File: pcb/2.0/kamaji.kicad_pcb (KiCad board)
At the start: 2 copper layers, 100 x 100 mm, 87 parts, among them J1 RJ10, J2 RJ10, J3 RJ10, J4 RJ10, J5 RJ10, J6 RJ10, J7 USB_B, J8 USB_A, Q1 2N3904, Q2 IRL540N, Q3 IRL540N, SW1 SW_Push, SW2 SW_Push, SW3 SW_Push, U1 ATMEGA32U4-AU, Y1 16MHz

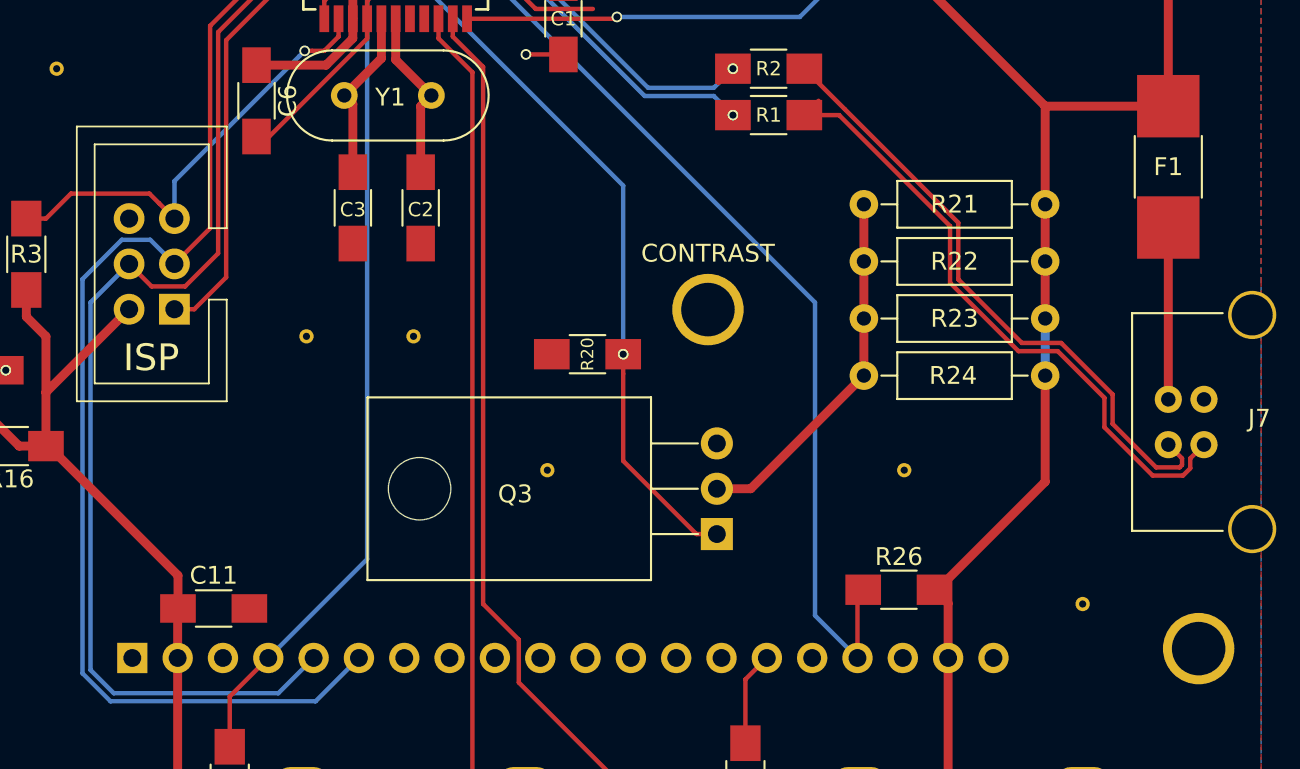
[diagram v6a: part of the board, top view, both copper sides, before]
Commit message: reroute the differential pair
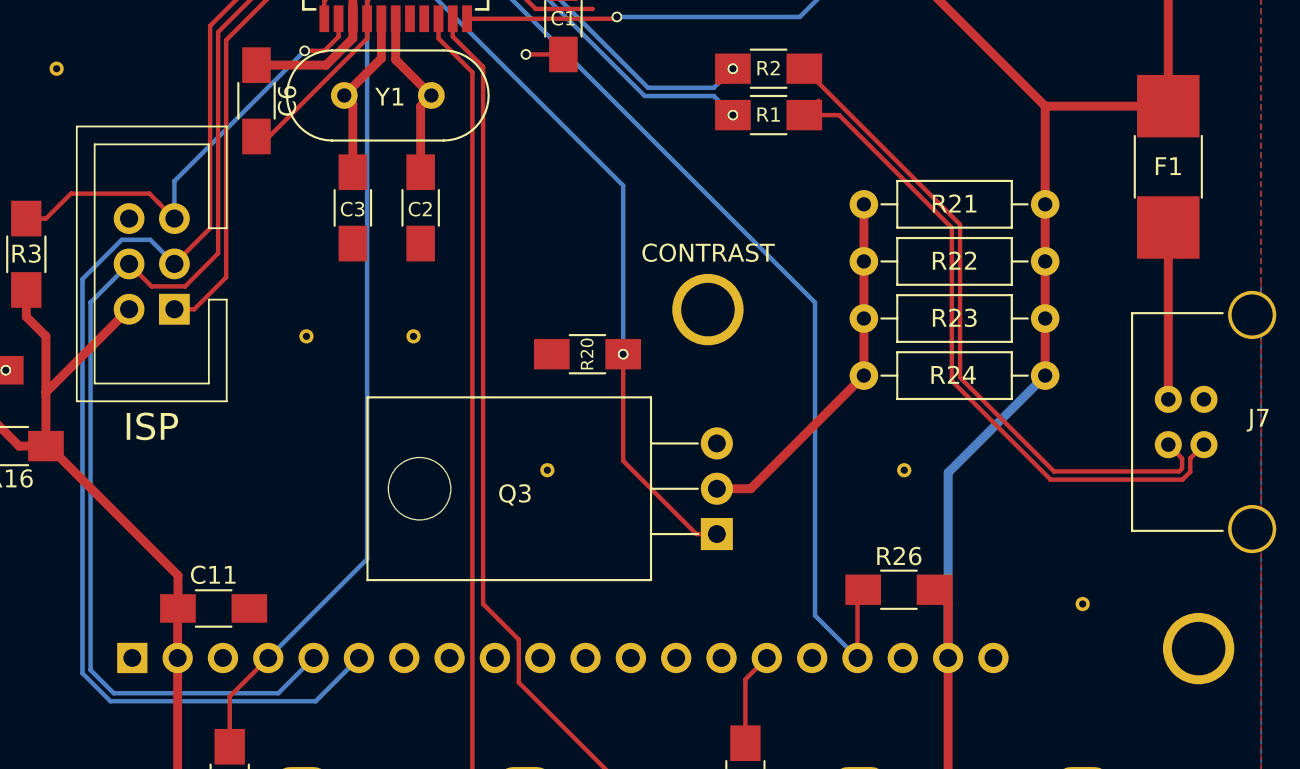
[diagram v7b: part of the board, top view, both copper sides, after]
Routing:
- net VCC: track 265.3 -> 268.9 mm
- net /USBBD-: track 34.8 -> 37.3 mm
- net /USBBD+: track 35.8 -> 38.3 mm
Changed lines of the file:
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@@
     (thickness 1.6)
     (drawings 15)
-    (tracks 395)
+    (tracks 387)
     (zones 0)
     (modules 87)
@@
     (effects (font (size 1 1) (thickness 0.2)))
   )
-  (gr_text ISP (at 85.3 116.2 360) (layer F.SilkS)
-    (effects (font (size 1.5 1.5) (thickness 0.3)))
+  (gr_text ISP (at 85.3 120.1) (layer F.SilkS)
+    (effects (font (size 1.5 1.5) (thickness 0.25)))
   )
   (gr_text 5V (at 73.25 107.8) (layer F.SilkS)
@@
   (segment (start 72.85 121.1) (end 75.35 121.1) (width 0.25) (layer F.Cu) (net 2))
   (segment (start 75.35 121.1) (end 75.4 121.15) (width 0.25) (layer F.Cu) (net 2))
+  (segment (start 129.961034 133.024284) (end 129.961034 122.638966) (width 0.5) (layer B.Cu) (net 3))
+  (segment (start 129.961034 122.638966) (end 135.4 117.2) (width 0.5) (layer B.Cu) (net 3))
+  (segment (start 135.4 117.2) (end 135.4 114) (width 0.5) (layer F.Cu) (net 3))
   (segment (start 103 85.8) (end 103 84.8) (width 0.5) (layer F.Cu) (net 3))
   (segment (start 103 84.8) (end 104.7 83.1) (width 0.5) (layer F.Cu) (net 3))
@@
   (segment (start 128.5 95.2) (end 109.7 95.2) (width 0.5) (layer F.Cu) (net 3))
   (segment (start 135.4 102.1) (end 128.5 95.2) (width 0.5) (layer F.Cu) (net 3))
-  (segment (start 135.4 114) (end 135.4 117.2) (width 0.5) (layer B.Cu) (net 3))
   (segment (start 129.961034 133.024284) (end 129.961034 145.438966) (width 0.5) (layer F.Cu) (net 3))
   (segment (start 129.961034 145.438966) (end 128 147.4) (width 0.5) (layer F.Cu) (net 3))
@@
   (segment (start 86.781034 133.024284) (end 86.781034 130.268966) (width 0.5) (layer F.Cu) (net 3))
   (segment (start 86.781034 130.268966) (end 86.8 130.25) (width 0.5) (layer F.Cu) (net 3))
-  (segment (start 135.4 117.2) (end 135.4 123.15) (width 0.5) (layer F.Cu) (net 3))
   (segment (start 129.35 129.2) (end 129.2 129.2) (width 0.5) (layer F.Cu) (net 3))
-  (segment (start 135.4 123.15) (end 129.35 129.2) (width 0.5) (layer F.Cu) (net 3))
   (segment (start 135.4 107.6) (end 135.4 110.8) (width 0.5) (layer F.Cu) (net 3))
   (segment (start 142.3 102.1) (end 142.3 87.39) (width 0.5) (layer F.Cu) (net 3))
@@
   (segment (start 65.9 114.4) (end 65.4 113.9) (width 0.5) (layer F.Cu) (net 51))
   (segment (start 124.174731 102.274731) (end 121.9 100) (width 0.25) (layer F.Cu) (net 52))
-  (segment (start 130.53 108.63) (end 124.174731 102.274731) (width 0.25) (layer F.Cu) (net 52))
-  (segment (start 130.53 111.804732) (end 130.53 108.63) (width 0.25) (layer F.Cu) (net 52))
-  (segment (start 134.095268 115.37) (end 130.53 111.804732) (width 0.25) (layer F.Cu) (net 52))
-  (segment (start 136.295268 115.37) (end 134.095268 115.37) (width 0.25) (layer F.Cu) (net 52))
-  (segment (start 139.18 118.254732) (end 136.295268 115.37) (width 0.25) (layer F.Cu) (net 52))
-  (segment (start 139.18 119.904732) (end 139.18 118.254732) (width 0.25) (layer F.Cu) (net 52))
-  (segment (start 141.61657 122.341302) (end 139.18 119.904732) (width 0.25) (layer F.Cu) (net 52))
-  (segment (start 142.93343 122.341302) (end 141.61657 122.341302) (width 0.25) (layer F.Cu) (net 52))
-  (segment (start 143.070001 122.204731) (end 142.93343 122.341302) (width 0.25) (layer F.Cu) (net 52))
-  (segment (start 143.070001 121.840001) (end 143.070001 122.204731) (width 0.25) (layer F.Cu) (net 52))
+  (segment (start 130.63 117.304732) (end 130.63 108.73) (width 0.25) (layer F.Cu) (net 52))
+  (segment (start 130.63 108.73) (end 124.174731 102.274731) (width 0.25) (layer F.Cu) (net 52))
+  (segment (start 135.895268 122.57) (end 130.63 117.304732) (width 0.25) (layer F.Cu) (net 52))
+  (segment (start 142.904732 122.57) (end 135.895268 122.57) (width 0.25) (layer F.Cu) (net 52))
+  (segment (start 143.070001 122.404731) (end 142.904732 122.57) (width 0.25) (layer F.Cu) (net 52))
   (segment (start 142.3 121.07) (end 143.070001 121.840001) (width 0.25) (layer F.Cu) (net 52))
+  (segment (start 143.070001 121.840001) (end 143.070001 122.404731) (width 0.25) (layer F.Cu) (net 52))
+  (segment (start 130.17 117.495268) (end 130.17 108.920538) (width 0.25) (layer F.Cu) (net 53))
   (segment (start 123.849462 102.6) (end 121.9 102.6) (width 0.25) (layer F.Cu) (net 53))
-  (segment (start 130.07 108.820538) (end 123.849462 102.6) (width 0.25) (layer F.Cu) (net 53))
-  (segment (start 130.07 111.995268) (end 130.07 108.820538) (width 0.25) (layer F.Cu) (net 53))
-  (segment (start 133.904732 115.83) (end 130.07 111.995268) (width 0.25) (layer F.Cu) (net 53))
-  (segment (start 136.104732 115.83) (end 133.904732 115.83) (width 0.25) (layer F.Cu) (net 53))
-  (segment (start 138.72 118.445268) (end 136.104732 115.83) (width 0.25) (layer F.Cu) (net 53))
-  (segment (start 138.72 120.095268) (end 138.72 118.445268) (width 0.25) (layer F.Cu) (net 53))
-  (segment (start 141.426034 122.801302) (end 138.72 120.095268) (width 0.25) (layer F.Cu) (net 53))
-  (segment (start 143.123966 122.801302) (end 141.426034 122.801302) (width 0.25) (layer F.Cu) (net 53))
-  (segment (start 143.529999 122.395269) (end 143.123966 122.801302) (width 0.25) (layer F.Cu) (net 53))
-  (segment (start 143.529999 121.840001) (end 143.529999 122.395269) (width 0.25) (layer F.Cu) (net 53))
+  (segment (start 130.17 108.920538) (end 123.849462 102.6) (width 0.25) (layer F.Cu) (net 53))
+  (segment (start 135.704732 123.03) (end 130.17 117.495268) (width 0.25) (layer F.Cu) (net 53))
+  (segment (start 143.095268 123.03) (end 135.704732 123.03) (width 0.25) (layer F.Cu) (net 53))
+  (segment (start 143.529999 122.595269) (end 143.095268 123.03) (width 0.25) (layer F.Cu) (net 53))
   (segment (start 144.3 121.07) (end 143.529999 121.840001) (width 0.25) (layer F.Cu) (net 53))
+  (segment (start 143.529999 121.840001) (end 143.529999 122.595269) (width 0.25) (layer F.Cu) (net 53))
   (segment (start 122.7 101.8) (end 121.9 102.6) (width 0.25) (layer F.Cu) (net 53))
   (segment (start 99.8 85.8) (end 99.8 83.75) (width 0.25) (layer F.Cu) (net 54))

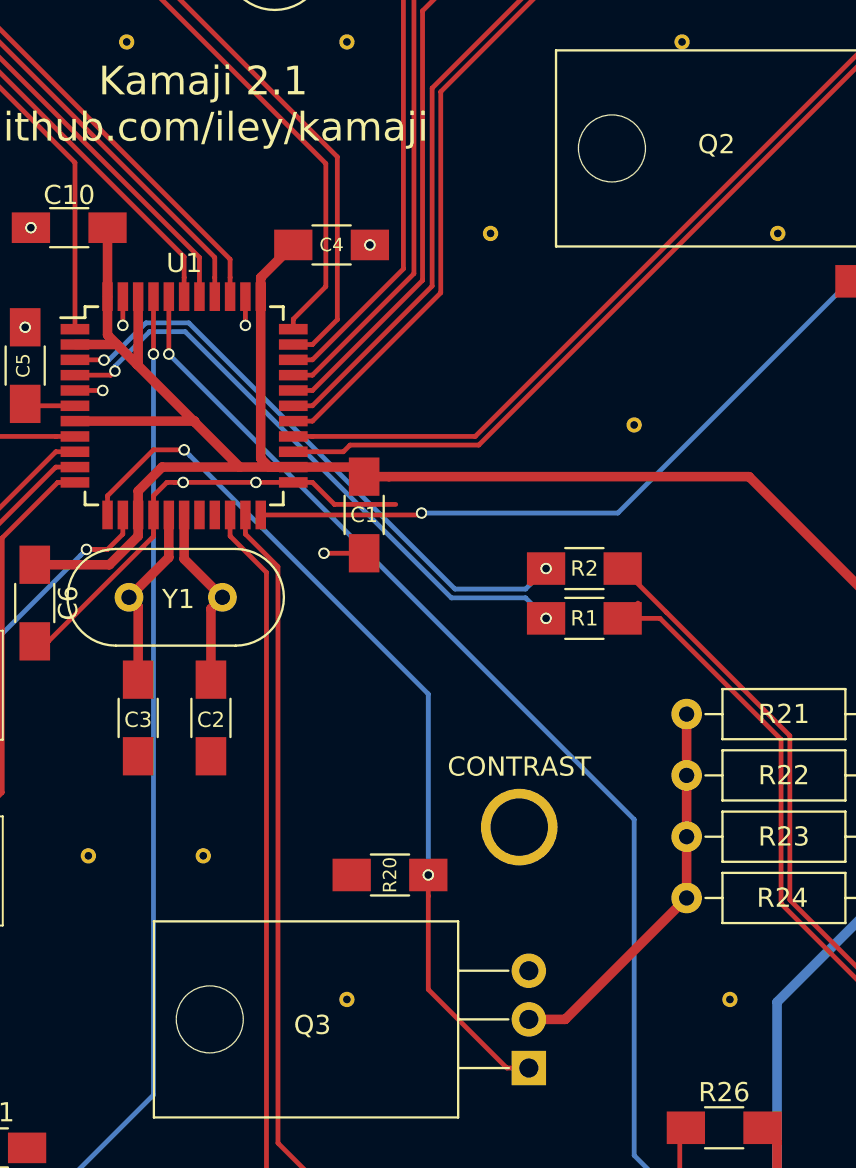
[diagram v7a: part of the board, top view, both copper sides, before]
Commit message: get rid of the holes on the TO-220 footprints
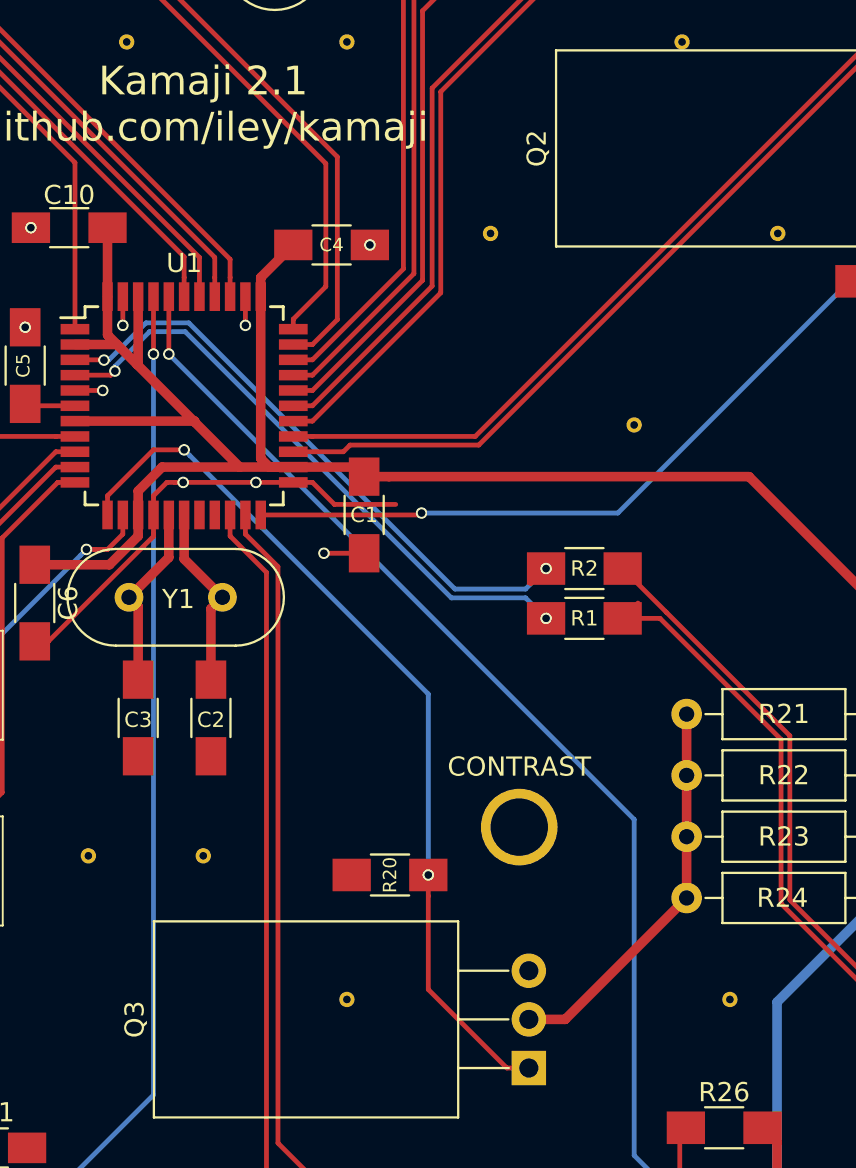
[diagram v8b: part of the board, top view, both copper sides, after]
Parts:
- Q2, Q3: footprint TO_SOT_Packages_THT:TO-220-3_Horizontal -> kamaji:TO-220-3_Horizontal
